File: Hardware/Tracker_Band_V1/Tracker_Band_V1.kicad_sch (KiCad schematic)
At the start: 51 parts, among them J1 USB_C_USB20, Q1 SSM6L56FE, SW1 EVP-AVAA1A, SW2 EVP-AVAA1A, U1 ESP32-C3-MINI-1-N4, U2 BNO085, U3 RT8010, U4 MCP73832-2-AC, U5 LM66200, U6 IN-PI15TAT5R5G5B, U7 IN-PI15TAT5R5G5B, U8 IN-PI15TAT5R5G5B, U9 IN-PI15TAT5R5G5B, X1 32.768kHz

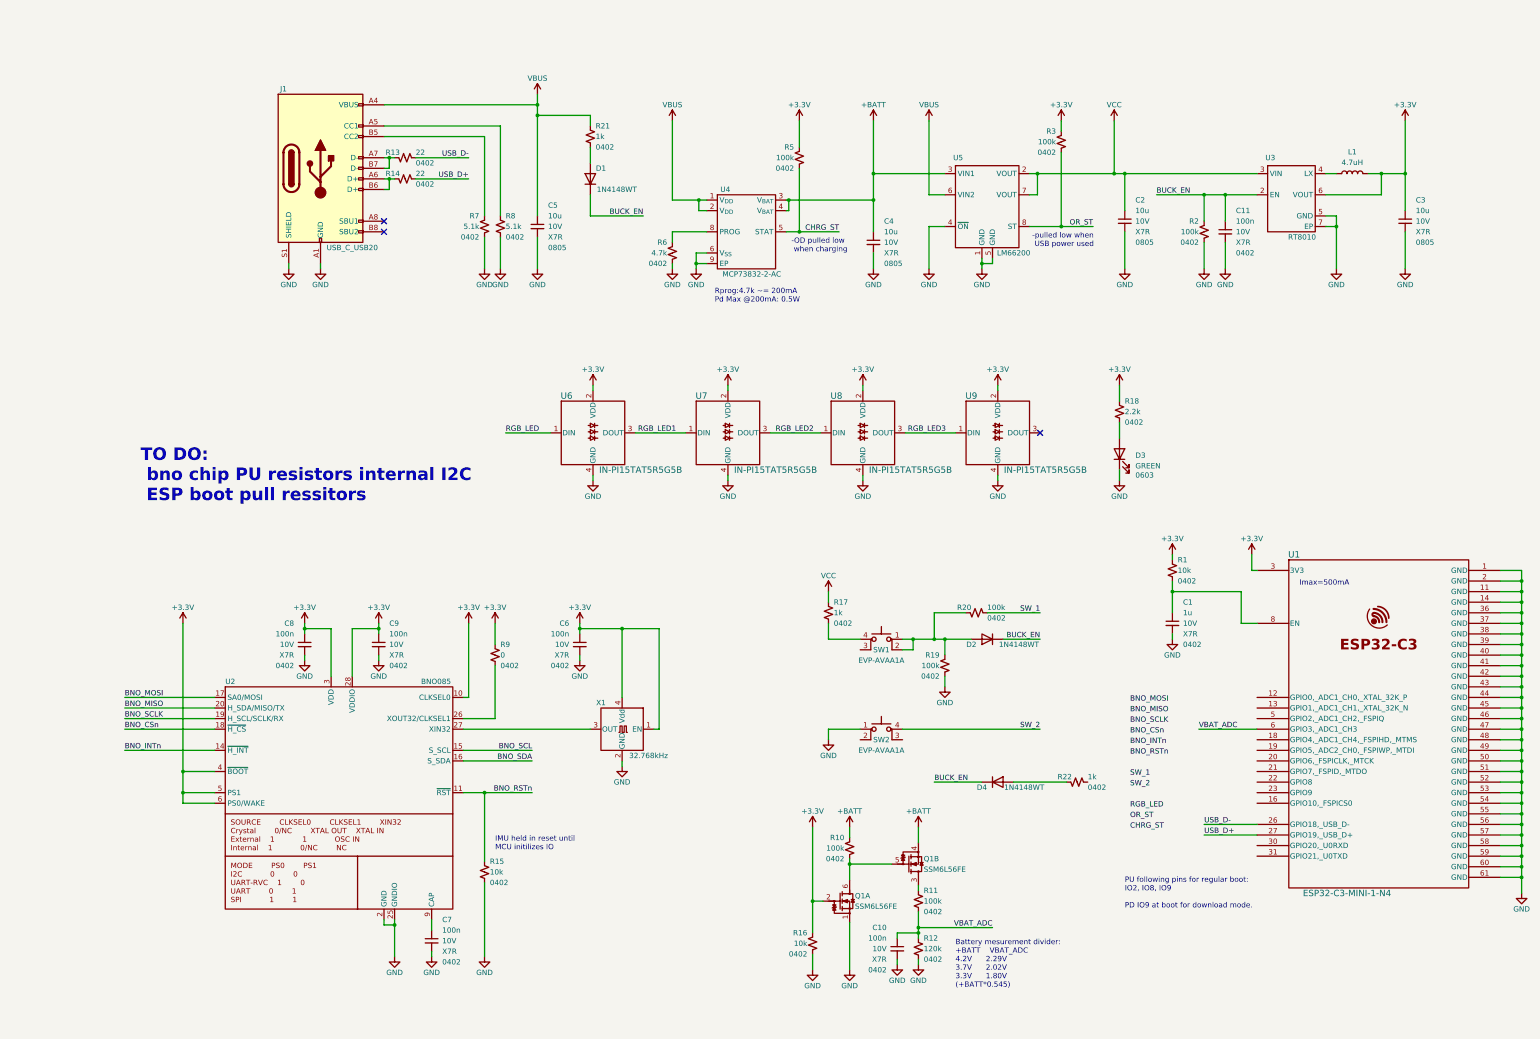
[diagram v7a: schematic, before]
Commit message: Started layout
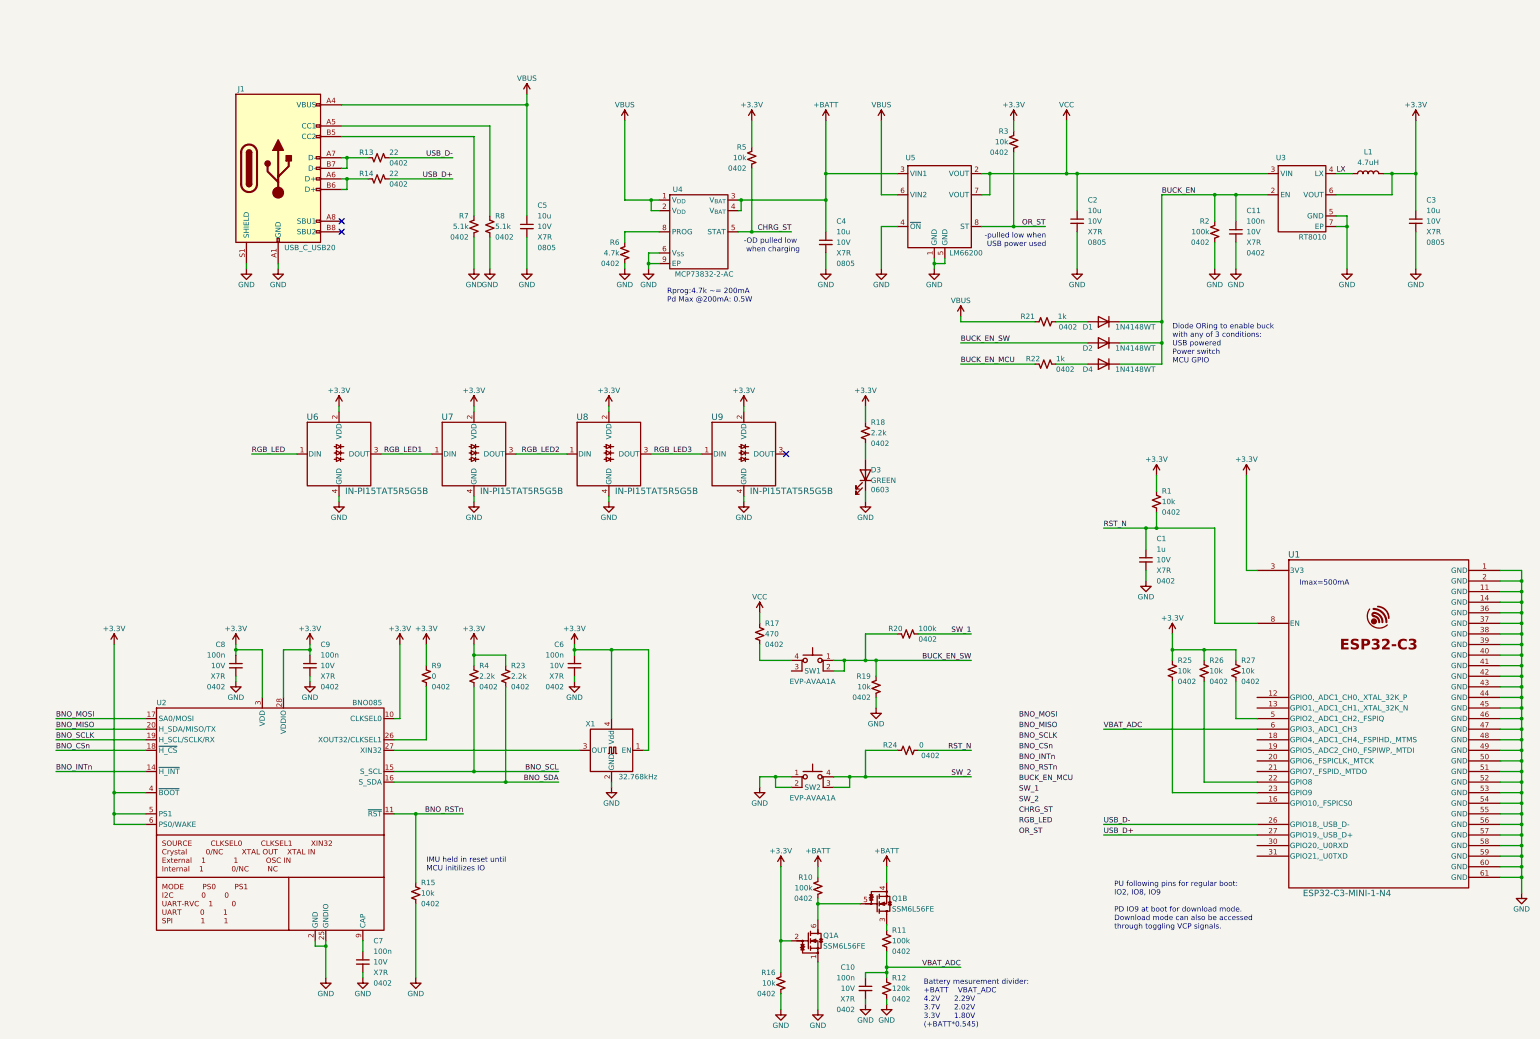
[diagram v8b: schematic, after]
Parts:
- added R23, R4: 2.2k, Resistor_SMD:R_0402_1005Metric, symbol Device:R_Small_US
- added R24: 0, Resistor_SMD:R_0402_1005Metric, symbol Device:R_Small_US
- added R25, R26, R27: 10k, Resistor_SMD:R_0402_1005Metric, symbol Device:R_Small_US
- R17: value 1k -> 470
- R19, R3, R5: value 100k -> 10k
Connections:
- net +3.3V: now also R23.1, R25.1, R26.1, R27.1, R4.1
- net BNO_SCL: now also R4.2
- net BNO_SDA: now also R23.2
- net GND: now also SW2.2
- net SW_2: now also SW2.3 (K), R24.1
- net BUCK_EN_SW: now reaches D2.2 (A), R19.1, R20.1, SW1.1, SW1.2
- net RST_N: now reaches C1.1, R1.2, U1.8 (EN)
- net RST_N: now also R24.2
- net LX: now reaches L1.1, U3.4 (LX)
- net at D4.2 (A): now also R22.2; no longer R22.1
- net at U1.22 (GPIO8): now also R26.2
- net at U1.23 (GPIO9): now also R25.2
- net at U1.5 (GPIO2,_ADC1_CH2,_FSPIQ): now also R27.2
- new net BUCK_EN_MCU: R22.1
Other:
- note added: "Diode ORing to enable buck with any of 3 conditions: USB powered Power switch MCU GPIO"
- note added: "PU following pins for regular boot: IO2, IO8, IO9 PD IO9 at boot for download mode. Download mode can also be accessed through toggling VCP signals."
- note removed: "PU following pins for regular boot: IO2, IO8, IO9 PD IO9 at boot for download mode."
- note removed: "TO DO: bno chip PU resistors internal I2C ESP boot pull ressitors"
- moved on the sheet: C1, C10, C11, C2, C3, C4, C5, C6, C7, C8, C9, D1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
